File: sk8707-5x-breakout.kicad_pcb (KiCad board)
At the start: 2 copper layers, 21.2 x 20.1 mm, 8 parts, among them J1 Conn_01x08_Socket, J2 Conn_01x04_Pin

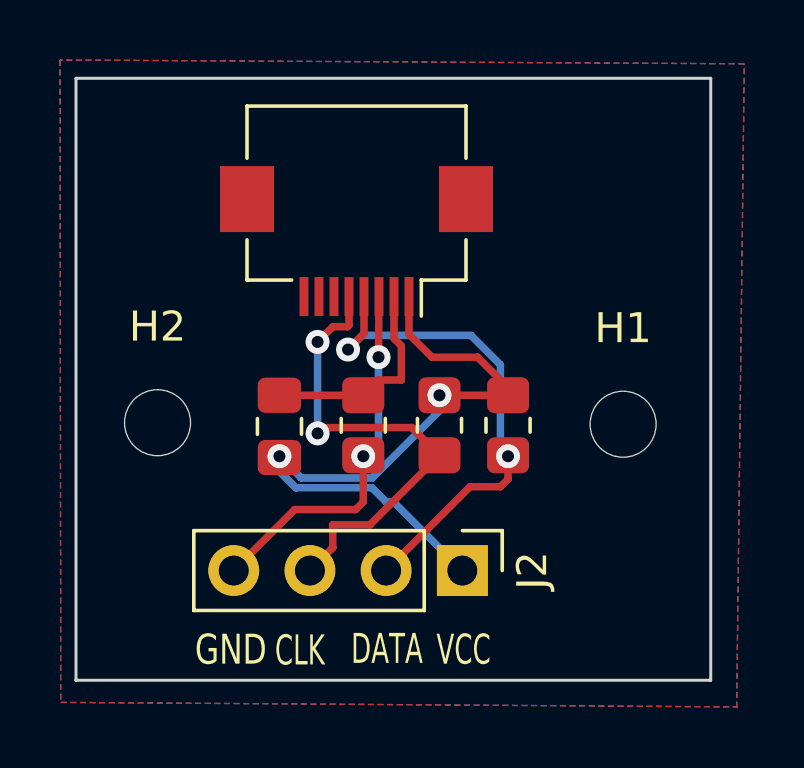
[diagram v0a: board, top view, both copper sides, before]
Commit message: edited routing and grounded mounting holes
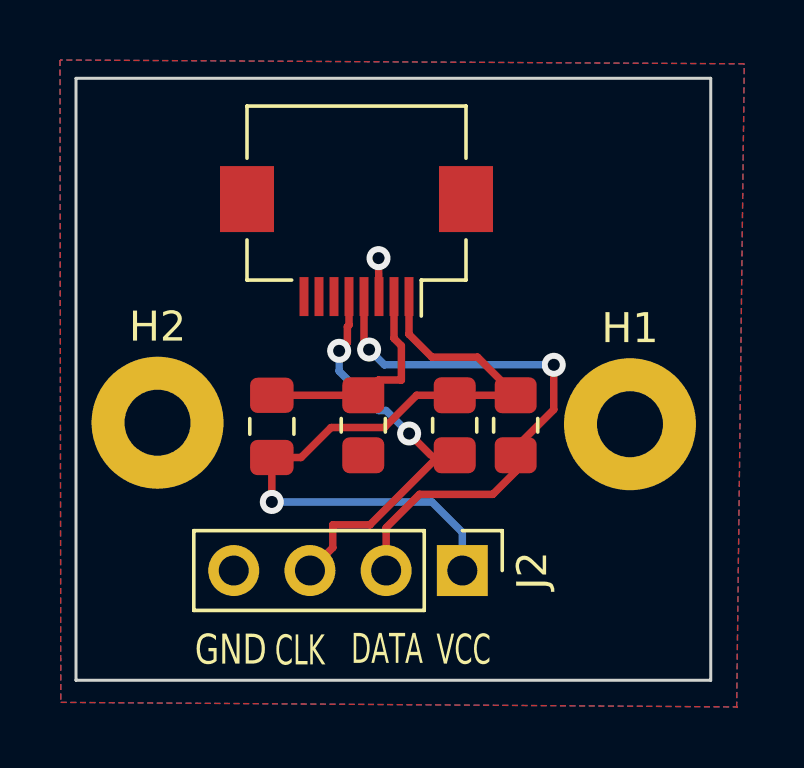
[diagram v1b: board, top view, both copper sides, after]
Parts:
- H1, H2: footprint MountingHole:MountingHole_2.2mm_M2 -> MountingHole:MountingHole_2.2mm_M2_Pad
- moved R2 0.51 mm to (134.9, 57.9)
- moved C1 0.25 mm to (128.8, 57.9)
- moved R1 0.25 mm to (136.9, 57.9)
- moved H1 0.23 mm to (140.7, 57.9)
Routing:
- net GND: track 12.2 -> 1.34 mm, vias 2 -> 1
- net CLK: track 16.2 -> 13.2 mm
- net DATA: track 16.8 -> 18.8 mm
- net VCC: track 22.9 -> 24.1 mm, vias 2 -> 1

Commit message: reversed pin order and grounded ffc connector
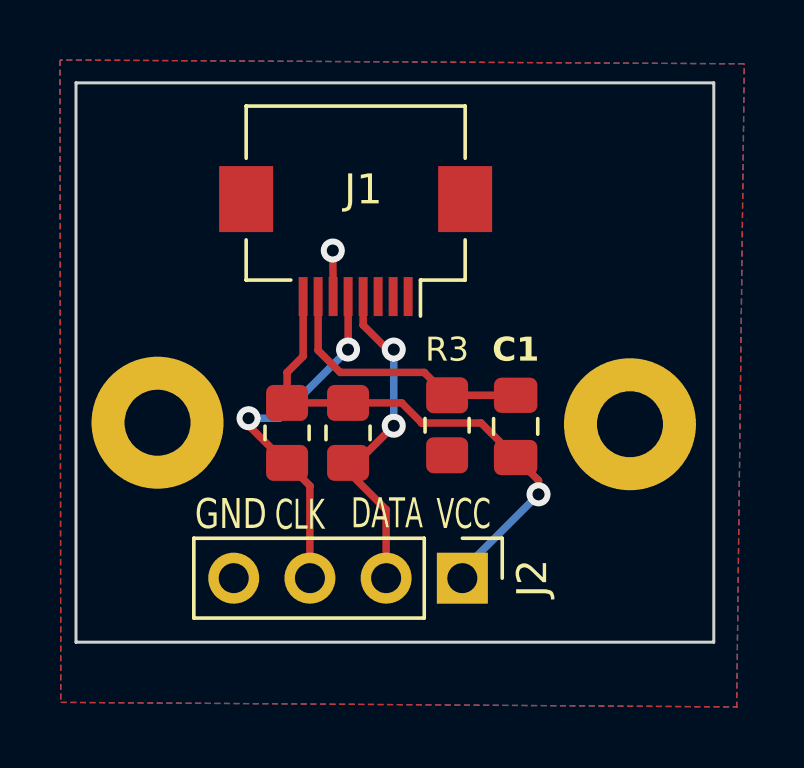
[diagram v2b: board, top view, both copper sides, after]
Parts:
- moved C1 8.13 mm to (136.9, 57.9)
- moved R1 7.62 mm to (129.3, 58.1)
- moved R2 3.57 mm to (131.3, 58.1)
- moved R3 2.79 mm to (134.6, 57.9)
- moved J2 0.25 mm to (135.1, 63.0)
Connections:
- J1 pad 1: VCC -> RIGHT
- J1 pad 2: IPD RST -> MIDDLE
- J1 pad 3: GND -> LEFT
- J1 pad 4: DATA -> CLK
- J1 pad 5: CLK -> DATA
- J1 pad 6: LEFT -> GND
- J1 pad 7: MIDDLE -> IPD RST
- J1 pad 8: RIGHT -> VCC
- J1 pad MP: (no net) -> GND
- J2 pad 2: DATA -> CLK
- J2 pad 3: CLK -> DATA
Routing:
- net DATA: track 18.8 -> 11.6 mm
- net VCC: track 24.1 -> 17.5 mm
- net CLK: track 13.2 -> 11.2 mm
- net IPD RST: track 7.16 -> 9.00 mm
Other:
- board size 21.2 x 20.1 mm -> 21.3 x 18.6 mm
- board text added: "https://github.com/KweBoakye/sk8707-5x-breakout"
- board text added: "sk8707-5x-breakout board v1.0"

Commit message: added trackpoint silkscreen icon, source image https://www.reddit.com/r/thinkpad/comments/8arjci/wanted_to_share_a_minimalist_trackpoint_wallpaper/
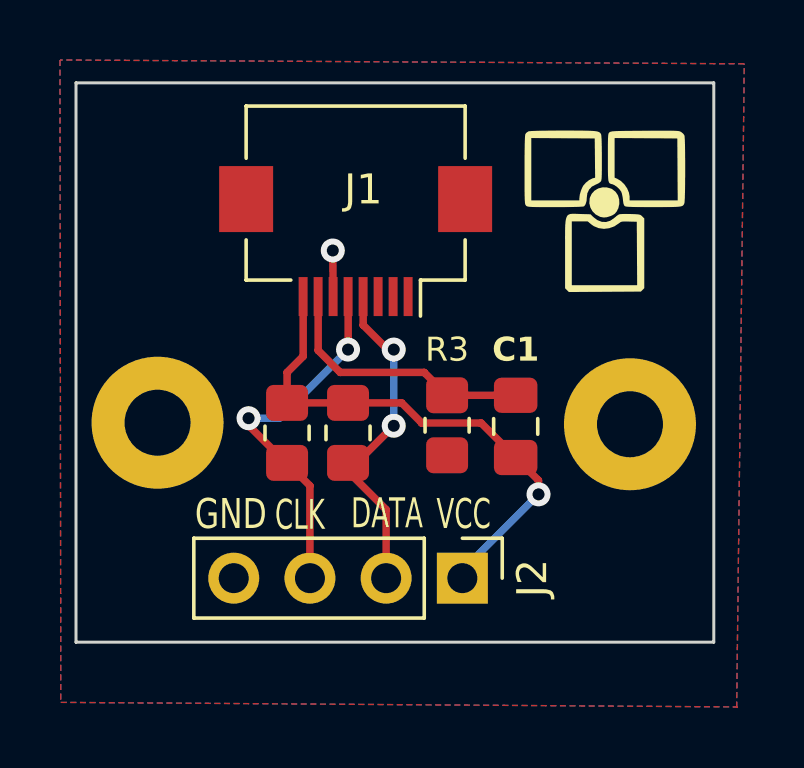
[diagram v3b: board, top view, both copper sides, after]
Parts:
- added G***: LOGO, project:trackpoint, F.Cu at (140.0, 50.8)
